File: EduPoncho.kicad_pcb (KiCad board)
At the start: 2 copper layers, 85.7 x 60.3 mm, 5 parts

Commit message: Correcion de errores, asignacion de footprints y ubicacion prelimilar de componentes.
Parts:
- removed MP?: Plantilla_EDU-CIAA, footprint:Plantilla_EDU-CIAA
- removed XA101: Conn_Poncho2P_2x_20x2, footprint:Conn_Poncho_SinBorde
- added D1: LL4148, Diodes_SMD:MiniMELF_Handsoldering, F.Cu at (97.5, 125.0)
- added D2: Led Rojo, LEDs:LED_0603, F.Cu at (93.5, 120.5)
- added D3: LL4148, Diodes_SMD:MiniMELF_Handsoldering, F.Cu at (97.5, 112.5)
- added D4: Led Rojo, LEDs:LED_0603, F.Cu at (93.5, 108.0)
- added D5: Led Verde, LEDs:LED_0603, F.Cu at (-78.6, 143.8)
- added D6: Led Verde, LEDs:LED_0603, F.Cu at (-55.5, 130.9)
- added D7: LL4148, Diodes_SMD:MiniMELF_Handsoldering, F.Cu at (117.8, 96.2)
- added Enc_r1: Encoder_rotativo, Potentiometers:Potentiometer_Alps-RK16-single_largePads, F.Cu at (63.5, 101.5)
- added J1: TB_1X3, Terminal_Blocks:TerminalBlock_Pheonix_PT-3.5mm_3pol, F.Cu at (65.6, 120.9)
- added J2: TB_1X3, Terminal_Blocks:TerminalBlock_Pheonix_PT-3.5mm_3pol, F.Cu at (65.6, 109.6)
- added J3: TB_1X3, Terminal_Blocks:TerminalBlock_Pheonix_PT-3.5mm_3pol, F.Cu at (-85.0, 62.0)
- added Q1: NDS7002A, TO_SOT_Packages_SMD:SOT-23_Handsoldering, F.Cu at (103.0, 126.5)
- added Q2: NDS7002A, TO_SOT_Packages_SMD:SOT-23_Handsoldering, F.Cu at (103.0, 114.5)
- added Q3: BC849, TO_SOT_Packages_SMD:SOT-23_Handsoldering, F.Cu at (128.0, 86.2)
- added R1: 330, Resistors_SMD:R_1206_HandSoldering, F.Cu at (93.5, 126.0)
- added R10: 4K7, Resistors_SMD:R_1206_HandSoldering, F.Cu at (-39.8, 131.7)
- added R11: 2K2, Resistors_SMD:R_1206_HandSoldering, F.Cu at (-43.4, 138.9)
- added R12: 100K, Resistors_SMD:R_1206_HandSoldering, F.Cu at (-25.7, 123.7)
- added R13: 2K2, Resistors_SMD:R_1206_HandSoldering, F.Cu at (-51.0, 138.9)
- added R14: 100K, Resistors_SMD:R_1206_HandSoldering, F.Cu at (-14.6, 106.1)
- added R15: 220, Resistors_SMD:R_1206_HandSoldering, F.Cu at (-25.7, 116.4)
- added R16: 4K7, Resistors_SMD:R_1206_HandSoldering, F.Cu at (-58.7, 142.0)
- added R17: 5K, Potentiometers:Potentiometer_Alps-RK16-single_largePads, F.Cu at (35.5, 67.0)
- added R18: 3K3, Resistors_SMD:R_1206_HandSoldering, F.Cu at (125.5, 94.2)
- added R2: 330, Resistors_SMD:R_1206_HandSoldering, F.Cu at (93.5, 113.5)
- added R3: 100K, Resistors_SMD:R_1206_HandSoldering, F.Cu at (103.0, 121.5)
- added R4: 100K, Resistors_SMD:R_1206_HandSoldering, F.Cu at (103.0, 109.0)
- added R5: 4K7, Resistors_SMD:R_1206_HandSoldering, F.Cu at (-18.0, 116.4)
- added R6: 3K3, Resistors_SMD:R_1206_HandSoldering, F.Cu at (-25.7, 131.0)
- added R7: 3K3, Resistors_SMD:R_1206_HandSoldering, F.Cu at (-35.7, 138.9)
- added R8: 4K7, Resistors_SMD:R_1206_HandSoldering, F.Cu at (-18.0, 123.7)
- added R9: 4K7, Resistors_SMD:R_1206_HandSoldering, F.Cu at (-47.4, 131.7)
- added RL1: G5Q-1, Relay_SPDT_Omron-G5-Q1, F.Cu at (88.4, 120.9)
- added RL2: G5Q-1, footprint:Relay_SPDT_Omron-G5-Q1, F.Cu at (88.4, 108.4)
- added U1: PS2805-1, Opto-Devices:Optocoupler_SMD_HandSoldering_KPC357_LTV35x_PC357_SingleChannel, F.Cu at (-24.0, 103.0)
- added U2: PS2805-1, Opto-Devices:Optocoupler_SMD_HandSoldering_KPC357_LTV35x_PC357_SingleChannel, F.Cu at (-65.4, 133.0)
- added U3: CNY70, footprint:CNY70, F.Cu at (-66.6, 142.5)
- added U4: Buzzer, Buzzers_Beepers:Buzzer_12x9.5RM7.6, F.Cu at (117.5, 87.8)
- added XA1: Conn_Poncho2P_2x_20x2, footprint:Conn_Poncho_Derecha, F.Cu at (137.2, 86.3)
- moved G*** 172.6 mm to (158.1, 254.8)
- moved G101 166.3 mm to (182.2, 250.3)
- moved G*** 151.4 mm to (172.6, 250.6)
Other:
- board text added: "Grilla de posicionamiento: 0,5mm"
- board text removed: "PONCHO BASICO http://www.proyecto-ciaa.com.ar/"

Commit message: Se agruparon componentes por bloques funcionales. Falta definir contorno de la placa y posicion final de los bloques.
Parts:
- moved U3 195.5 mm to (128.1, 159.5)
- moved R16 194.0 mm to (134.5, 159.5), turned to 90 degrees
- moved J3 178.7 mm to (61.0, 165.0), turned to 270 degrees
- moved D5 164.2 mm to (82.0, 178.0), turned to 90 degrees
- moved R15 154.3 mm to (122.5, 159.5), turned to 90 degrees
- moved U2 139.6 mm to (72.0, 157.5), turned to 90 degrees
- moved R9 139.5 mm to (77.0, 68.5), turned to 270 degrees
- moved D6 139.1 mm to (81.0, 157.5), turned to 270 degrees
- moved R13 128.9 mm to (76.5, 157.5), turned to 270 degrees
- moved R11 124.6 mm to (72.0, 186.0)
- moved U1 121.8 mm to (72.0, 178.0), turned to 90 degrees
- moved R10 116.9 mm to (72.0, 166.0)
- moved R12 116.6 mm to (77.5, 178.0), turned to 270 degrees
- moved R5 110.2 mm to (77.0, 60.5), turned to 90 degrees
- moved R7 104.4 mm to (67.0, 157.5), turned to 90 degrees
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
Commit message: Se definió contorno de la placa y se ubicaron los componentes. También se ruteo la placa completa, falta revisión
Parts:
- added G***: LOGO, footprint:Logo_Poncho, F.Cu at (186.0, 111.5)
- added G***: LOGO, footprint:Logo_Poncho, F.Cu at (102.0, 171.5)
- added MP?: Plantilla_EDU-CIAA, footprint:Plantilla_EDU-CIAA, F.Cu at (138.7, 86.3)
- moved G*** 131.8 mm to (244.6, 155.3)
- moved G*** 131.8 mm to (259.1, 151.1)
- moved G101 131.8 mm to (268.7, 150.8)
- moved R8 86.6 mm to (91.0, 86.0)
- moved R11 86.1 mm to (91.8, 102.2)
- moved R12 86.1 mm to (97.3, 94.2)
- moved R6 86.1 mm to (87.3, 94.2)
- moved U1 86.1 mm to (91.8, 94.2)
- moved D5 79.2 mm to (71.5, 99.5), turned to 180 degrees
- moved J3 74.1 mm to (65.5, 91.0)
- moved D6 69.2 mm to (71.5, 89.0), turned to 180 degrees
- moved R10 63.5 mm to (76.8, 102.7)
- moved R13 63.5 mm to (81.3, 94.2)
- moved R14 63.5 mm to (77.3, 86.2)
- moved R7 63.5 mm to (71.8, 94.2)
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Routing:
- net +3V3: track 0.00 -> 337.7 mm, vias 0 -> 2
- net +5V: track 0.00 -> 163.2 mm
- net /Conector Poncho/Encoder_B: track 0.00 -> 146.8 mm, vias 0 -> 3
- net /Conector Poncho/OPTO_IN1: track 0.00 -> 115.3 mm, vias 0 -> 3
- net /Conector Poncho/Encoder_A: track 0.00 -> 114.7 mm, vias 0 -> 2
- net /Conector Poncho/Pote: track 0.00 -> 114.2 mm
- net /Conector Poncho/OPTO_IN0: track 0.00 -> 94.4 mm, vias 0 -> 1
- net /Conector Poncho/CNY_IN: track 0.00 -> 58.9 mm, vias 0 -> 1
- net /Conector Poncho/GPIO1: track 0.00 -> 53.6 mm, vias 0 -> 1
- net /Entradas/COM: track 0.00 -> 52.7 mm
- net /Conector Poncho/GPIO0: track 0.00 -> 43.2 mm
- net /Entradas/IN1: track 0.00 -> 36.6 mm
- net Net-(D5-Pad2): track 0.00 -> 31.4 mm, vias 0 -> 2
- net Net-(R6-Pad1): track 0.00 -> 22.0 mm, vias 0 -> 2
- net Net-(D3-Pad2): track 0.00 -> 21.0 mm
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- added copper zone on B.Cu, net GND
- added copper zone on F.Cu, net GND
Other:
- board size 85.7 x 60.3 mm -> 86 x 137.5 mm
- net class Default: clearance 0.51 -> 0.5; trace_width 0.381 -> 0.5; via_dia 0.6 -> 1.27; via_drill 0.4 -> 0.7112
- rule trace_clearance: 0.51 -> 0.5
- rule trace_min: 0.2 -> 0.5
- rule via_min_drill: 0.3 -> 0.7112
- rule via_min_size: 0.4 -> 1.27
- board text added: "Grilla de ruteo: 0,1mm"
- board text removed: "Editar el rótulo"

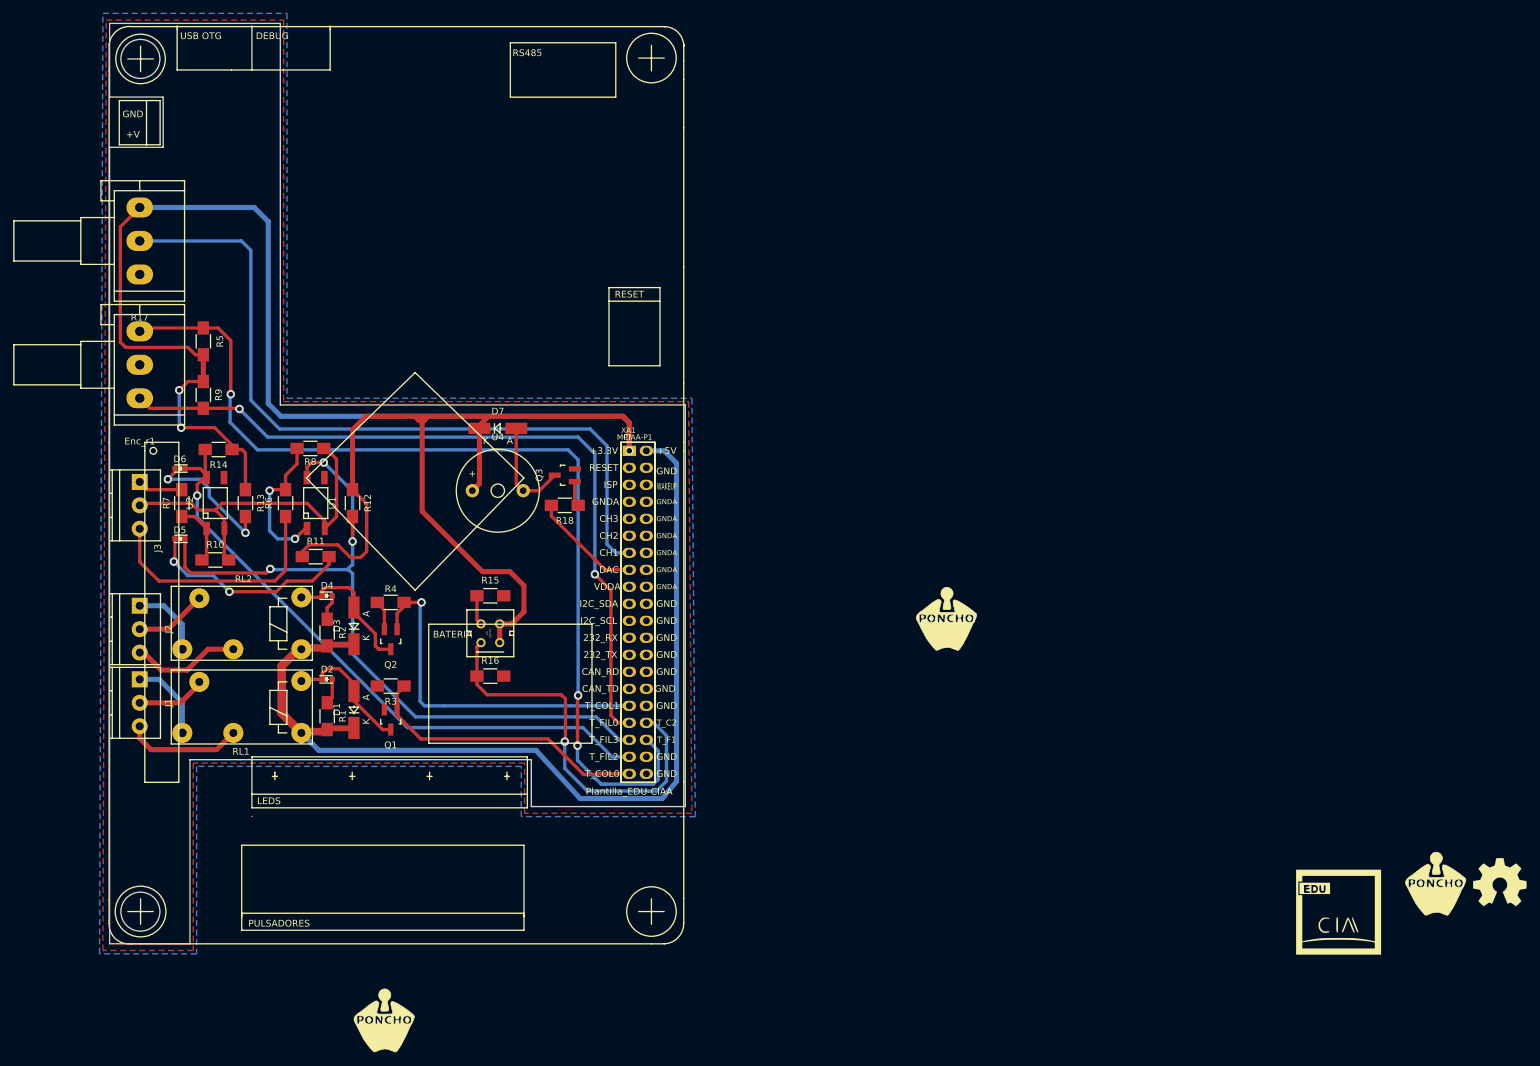
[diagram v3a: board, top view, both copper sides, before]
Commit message: Se termino de rutear la placa y se acomodaron ref de los componentes, se agrego nombres y fiduciales
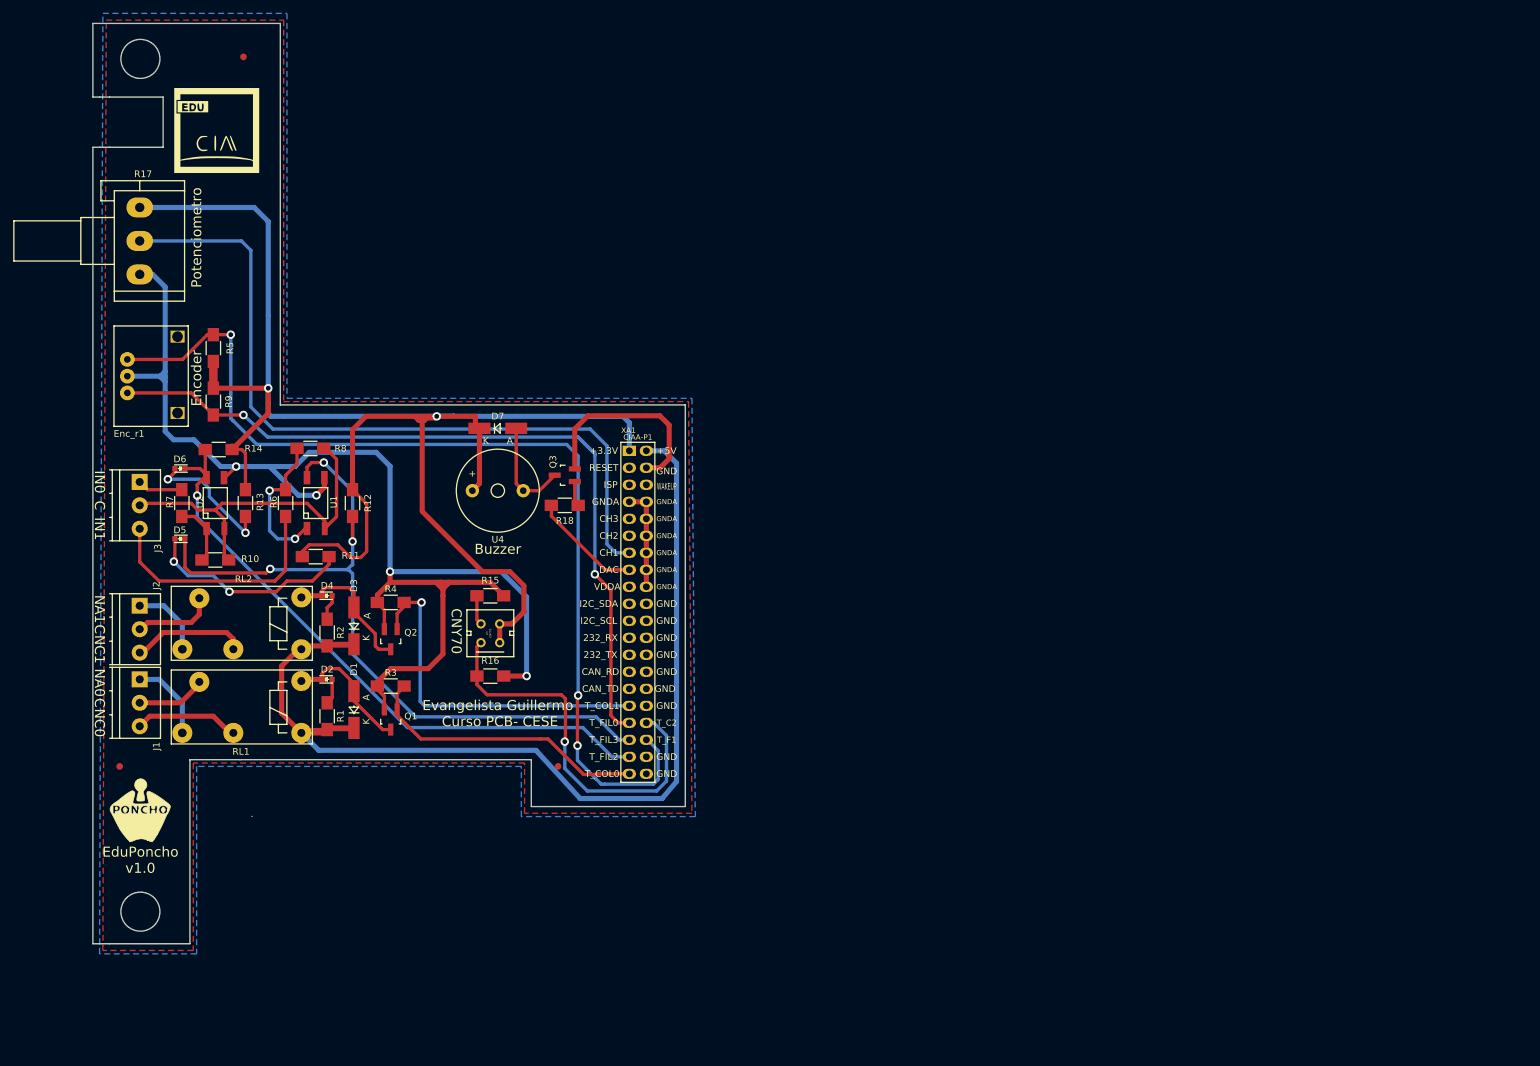
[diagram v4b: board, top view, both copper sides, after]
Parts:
- removed the G*** at (259.1, 151.1)
- removed the G*** at (186.0, 111.5)
- removed G101: Logo_OSHWA, footprint:Logo_OSHWA
- removed MP?: Plantilla_EDU-CIAA, footprint:Plantilla_EDU-CIAA
- added F?: Fiducial_1mm, footprint:Fiducial_1mm, F.Cu at (81.0, 27.5)
- added F?: Fiducial_1mm, footprint:Fiducial_1mm, F.Cu at (128.0, 133.5)
- added F?: Fiducial_1mm, footprint:Fiducial_1mm, F.Cu at (62.5, 133.5)
- moved G*** 204.3 mm to (77.0, 38.5)
- moved G*** 48.1 mm to (65.5, 140.1)
- moved Enc_r1 3.78 mm to (63.6, 75.2)
- moved R5 1.80 mm to (76.5, 71.0)
- moved R9 1.80 mm to (76.5, 79.0)
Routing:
- net GND: track 4.43 -> 228.2 mm, vias 0 -> 4
- net +3V3: track 337.7 -> 281.9 mm
- net GNDA: track 0.00 -> 15.2 mm
- net /Conector Poncho/Encoder_A: track 114.7 -> 120.5 mm
- net /Conector Poncho/Encoder_B: track 146.8 -> 149.9 mm
- net +5V: track 163.2 -> 160.6 mm
- net Net-(J2-Pad2): track 11.7 -> 13.9 mm
- net Net-(J1-Pad3): track 17.5 -> 15.6 mm
- net Net-(J2-Pad3): track 16.3 -> 17.7 mm
- net /Conector Poncho/Pote: track 114.2 -> 114.8 mm
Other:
- board size 86 x 137.5 mm -> 88.5 x 137.5 mm
- board text added: "Buzzer"
- board text added: "C"
- board text added: "CNY70"
- board text added: "Diseño doble faz. Sin requerimientos especiales."
- board text added: "EduPoncho v1.0"
- board text added: "Encoder"
- board text added: "Evangelista Guillermo Curso PCB- CESE"
- board text added: "IN0"
- board text added: "IN1"
- board text added: "NA0"
- board text added: "NA1"
- board text added: "NC0"
- board text added: "NC1"
- board text added: "Potenciometro"
- board text removed: "Borrar (Footprint MP1) la Plantilla-EDU-CIAA al finalizar el posicionamiento y definido el borde de PCB."
- board text removed: "Diseño simple faz. Sin requerimientos especiales."
- board text removed: "Editar este cuadro para reflejar cantidad de capas, si se han realizado cálculos de impedancia o si es relevante para el funcionamiento."
- board text removed: "Se sugiere colocar Nombre de Poncho y autor en cobre, serigrafía y rótulo."

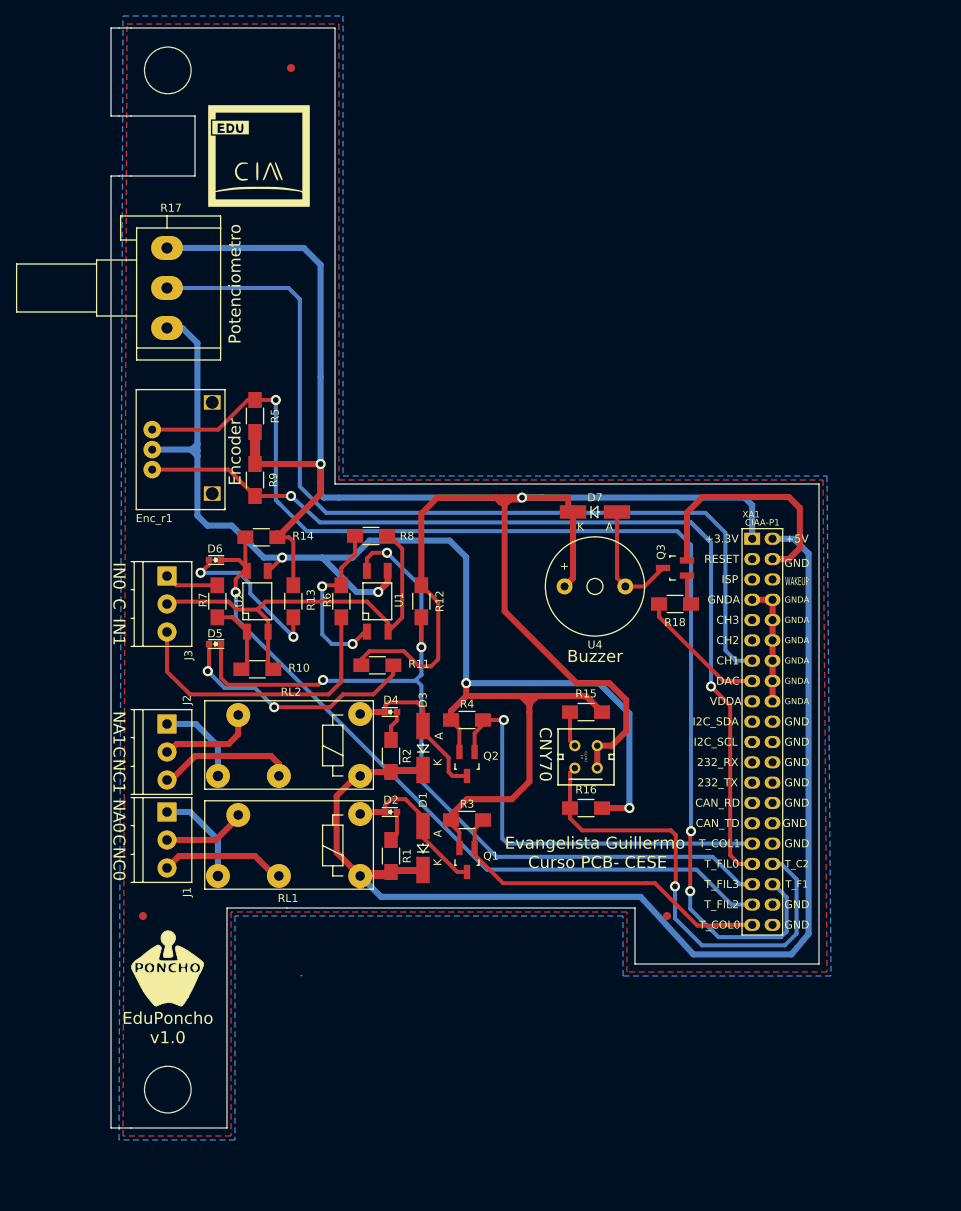
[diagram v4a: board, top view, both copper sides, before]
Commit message: Se agregaron cotas, fiducidales y escrituras en cobre. Tambien se corrigieron algunos errores.
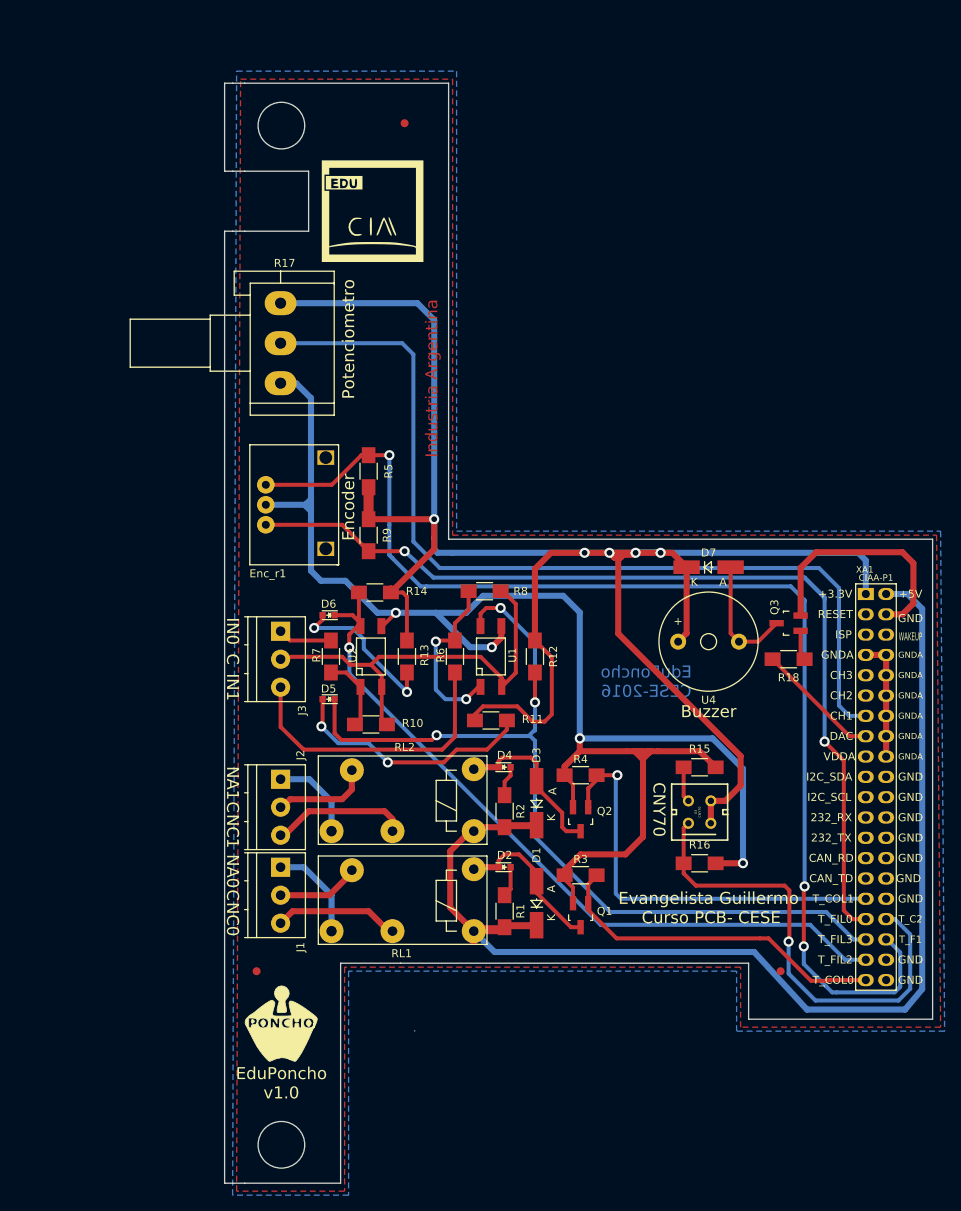
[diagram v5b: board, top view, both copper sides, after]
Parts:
- moved U3 15.8 mm to (132.1, 120.5)
- moved R15 15.8 mm to (132.1, 114.9)
- moved R16 15.8 mm to (132.1, 126.9)
- moved D1 15.8 mm to (111.7, 131.9)
- moved D2 15.8 mm to (107.7, 127.4)
- moved D3 15.8 mm to (111.7, 119.4)
- moved D4 15.8 mm to (107.7, 114.9)
- moved D5 15.8 mm to (85.7, 106.4)
- moved D6 15.8 mm to (85.7, 95.9)
- moved F? 15.8 mm to (76.7, 140.4)
- moved G*** 15.8 mm to (79.8, 147.0)
- moved J1 15.8 mm to (79.7, 127.4)
- moved J2 15.8 mm to (79.7, 116.4)
- moved J3 15.8 mm to (79.7, 97.9)
- moved Q1 15.8 mm to (117.2, 133.4)
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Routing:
- net +3V3: track 281.9 -> 283.1 mm, vias 2 -> 5
- net /Conector Poncho/Buzzer: track 16.6 -> 15.6 mm
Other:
- board text added: "Ancho minimo de pista 0,5mm Diametro agujero via 0,71mm Diametro de via 1,27mm"
- board text added: "EduPoncho CESE-2016"
- board text added: "Industria Argentina"
